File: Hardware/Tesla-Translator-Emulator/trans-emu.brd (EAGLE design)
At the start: 29 x 34 mm, 41 parts, among them IC1 MIC5233-3.3YM5-TR, Q1 PMOSFET, Q2 NMOSFET, U1 STM32F413RGT6, U2 TJA1042HVSON, U3 TJA1042HVSON, U4 TJA1042HVSON, Y1 CRYSTAL-3.2X2.54-PIN

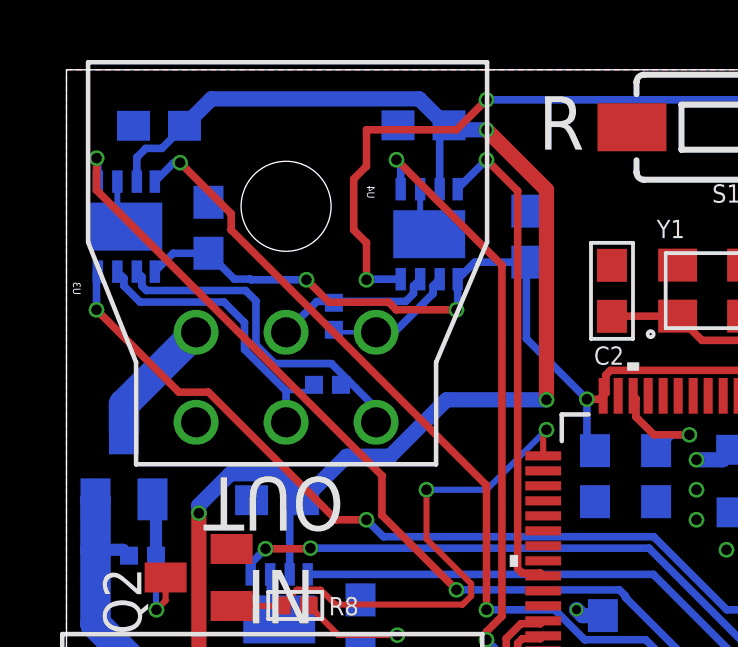
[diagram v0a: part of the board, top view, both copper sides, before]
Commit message: ibooster v2, stm32teensy work
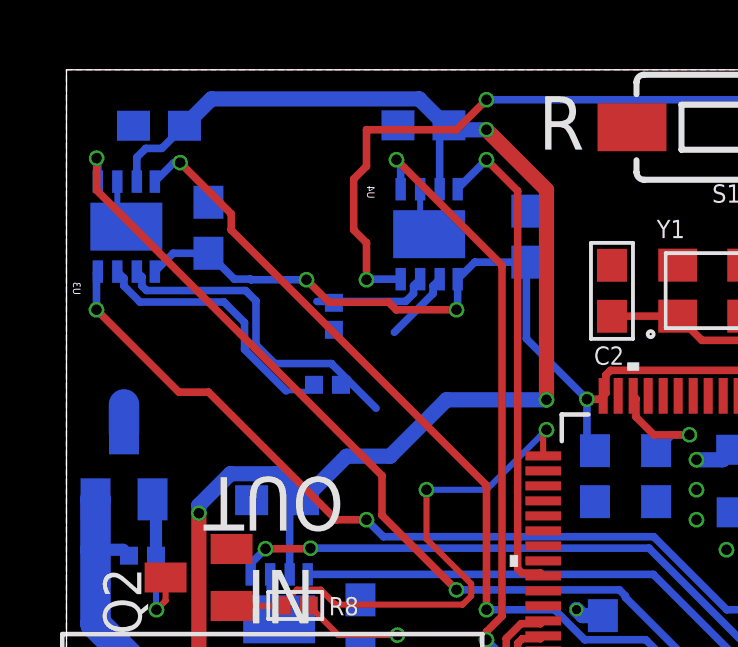
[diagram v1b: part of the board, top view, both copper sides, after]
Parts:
- removed U$2: MICROFIT-6, interceptor:MICROFIT-6
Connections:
- net CAN2_H: no longer U$2.2
- net CAN2_L: no longer U$2.3
- net CAN3_H: no longer U$2.5
- net CAN3_L: no longer U$2.6
- net GND: no longer U$2.1
- net N$15: no longer U$2.4
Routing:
- net N$15: track 4.36 -> 0.97 mm
- net CAN3_L: track 4.44 -> 2.40 mm
- net CAN3_H: track 5.46 -> 3.94 mm
- net CAN2_H: track 10.0 -> 8.97 mm
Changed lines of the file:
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@@
 </element>
 <element name="U$1" library="interceptor" package="MINI50" value="MINI50-4" x="9.86" y="12.19" smashed="yes" rot="R180"/>
-<element name="U$2" library="interceptor" package="MICROFIT-6" value="MICROFIT-6" x="7.32" y="22.25" smashed="yes" rot="R180"/>
 <element name="U1" library="interceptor" package="LQFP64-10X10MM" value="STM32F413RGT6" x="21.64" y="17.38" smashed="yes" rot="R180">
 <attribute name="BUILT_BY" value="EMA_UL_Team" x="-19" y="25" size="1.778" layer="27" rot="R180" display="off"/>
@@
 <contactref element="C14" pad="2"/>
 <contactref element="C12" pad="2"/>
-<contactref element="U$2" pad="1"/>
 <contactref element="IC1" pad="2"/>
 <contactref element="PS1" pad="2"/>
@@
 <wire x1="6.170878125" y1="19.65268125" x2="5.50338125" y2="18.02668125" width="0" layer="19" extent="1-16"/>
 <wire x1="9.86" y1="12.19" x2="11" y2="15" width="0" layer="19" extent="16-16"/>
-<wire x1="4.32" y1="22.25" x2="6.170878125" y2="19.65268125" width="0" layer="19" extent="16-16"/>
 <wire x1="7.278778125" y1="1.89358125" x2="12.39" y2="3.61" width="0" layer="19" extent="16-16"/>
 <wire x1="5.8147" y1="5.02721875" x2="7.278778125" y2="1.89358125" width="0" layer="19" extent="16-16"/>
@@
 <signal name="CAN2_H">
 <contactref element="U3" pad="7"/>
-<contactref element="U$2" pad="2"/>
 <wire x1="1.6952625" y1="27.27271875" x2="1.9162625" y2="27.05171875" width="0.254" layer="16"/>
 <wire x1="1.9162625" y1="27.05171875" x2="1.9162625" y2="26.79250625" width="0.254" layer="16"/>
@@
 <wire x1="5.25018125" y1="26.25851875" x2="5.935" y2="25.5737" width="0.254" layer="16"/>
 <wire x1="5.935" y1="25.5737" x2="5.935" y2="24.67630625" width="0.254" layer="16"/>
-<wire x1="7.32" y1="23.29130625" x2="7.32" y2="22.25" width="0.254" layer="16"/>
 <wire x1="5.935" y1="24.67630625" x2="7.32" y2="23.29130625" width="0.254" layer="16"/>
 <contactref element="R5" pad="1"/>
@@
 <signal name="CAN2_L">
 <contactref element="U3" pad="6"/>
-<contactref element="U$2" pad="3"/>
 <wire x1="2.3452625" y1="27.27271875" x2="2.5162625" y2="27.10171875" width="0.254" layer="16"/>
 <wire x1="2.5162625" y1="27.10171875" x2="2.5162625" y2="26.79250625" width="0.254" layer="16"/>
@@
 <wire x1="6.942225" y1="24.2079" x2="8.829878125" y2="24.2079" width="0.254" layer="16"/>
 <wire x1="6.316" y1="26.2976" x2="6.316" y2="24.834125" width="0.254" layer="16"/>
-<wire x1="10.32" y1="22.25" x2="10.32" y2="22.717778125" width="0.254" layer="16"/>
 <wire x1="10.32" y1="22.717778125" x2="9.364978125" y2="23.6728" width="0.254" layer="16"/>
 <contactref element="R5" pad="2"/>
@@
 <signal name="CAN3_H">
 <contactref element="U4" pad="7"/>
-<contactref element="U$2" pad="5"/>
 <wire x1="11.79" y1="27.02" x2="11.569" y2="26.799" width="0.254" layer="16"/>
 <wire x1="11.569" y1="26.799" x2="11.569" y2="26.5397875" width="0.254" layer="16"/>
 <wire x1="11.569" y1="26.5397875" x2="11.308053125" y2="26.278840625" width="0.254" layer="16"/>
-<wire x1="8.348840625" y1="26.278840625" x2="7.32" y2="25.25" width="0.254" layer="16"/>
 <wire x1="11.308053125" y1="26.278840625" x2="9" y2="26.278840625" width="0.254" layer="16"/>
+<wire x1="9" y1="26.278840625" x2="8.348840625" y2="26.278840625" width="0.254" layer="16"/>
+<wire x1="8.960459375" y1="26.278840625" x2="9" y2="26.278840625" width="0.1524" layer="16"/>
 <contactref element="R6" pad="1"/>
-<wire x1="9" y1="26.278840625" x2="8.348840625" y2="26.278840625" width="0.254" layer="16"/>
-<wire x1="8.9144" y1="26.23278125" x2="8.960459375" y2="26.278840625" width="0.1524" layer="16"/>
-<wire x1="8.960459375" y1="26.278840625" x2="9" y2="26.278840625" width="0.1524" layer="16"/>
+<wire x1="8.9144" y1="26.23278125" x2="8.960459375" y2="26.278840625" width="0" layer="19" extent="16-16"/>
 </signal>
 <signal name="CAN3_L">
 <contactref element="U4" pad="6"/>
-<contactref element="U$2" pad="6"/>
 <wire x1="12.44" y1="27.02" x2="12.219" y2="26.799" width="0.254" layer="16"/>
 <wire x1="12.219" y1="26.799" x2="12.219" y2="26.5397875" width="0.254" layer="16"/>
 <wire x1="12.219" y1="26.5397875" x2="10.9292125" y2="25.25" width="0.254" layer="16"/>
-<wire x1="10.9292125" y1="25.25" x2="10.32" y2="25.25" width="0.254" layer="16"/>
 <contactref element="R6" pad="2"/>
-<wire x1="10.32" y1="25.25" x2="8.99718125" y2="25.25" width="0.1524" layer="16"/>
-<wire x1="8.99718125" y1="25.25" x2="8.9144" y2="25.33278125" width="0.1524" layer="16"/>
+<wire x1="8.9144" y1="25.33278125" x2="10.9292125" y2="25.25" width="0" layer="19" extent="16-16"/>
 </signal>
 <signal name="N$2">
@@
 </signal>
 <signal name="N$15">
-<contactref element="U$2" pad="4"/>
 <contactref element="Q1" pad="3"/>
 <wire x1="1.917440625" y1="21.88231875" x2="1.917440625" y2="22.847440625" width="1.016" layer="16"/>
-<wire x1="1.917440625" y1="22.847440625" x2="4.32" y2="25.25" width="1.016" layer="16"/>
 </signal>
 <signal name="PWRON">

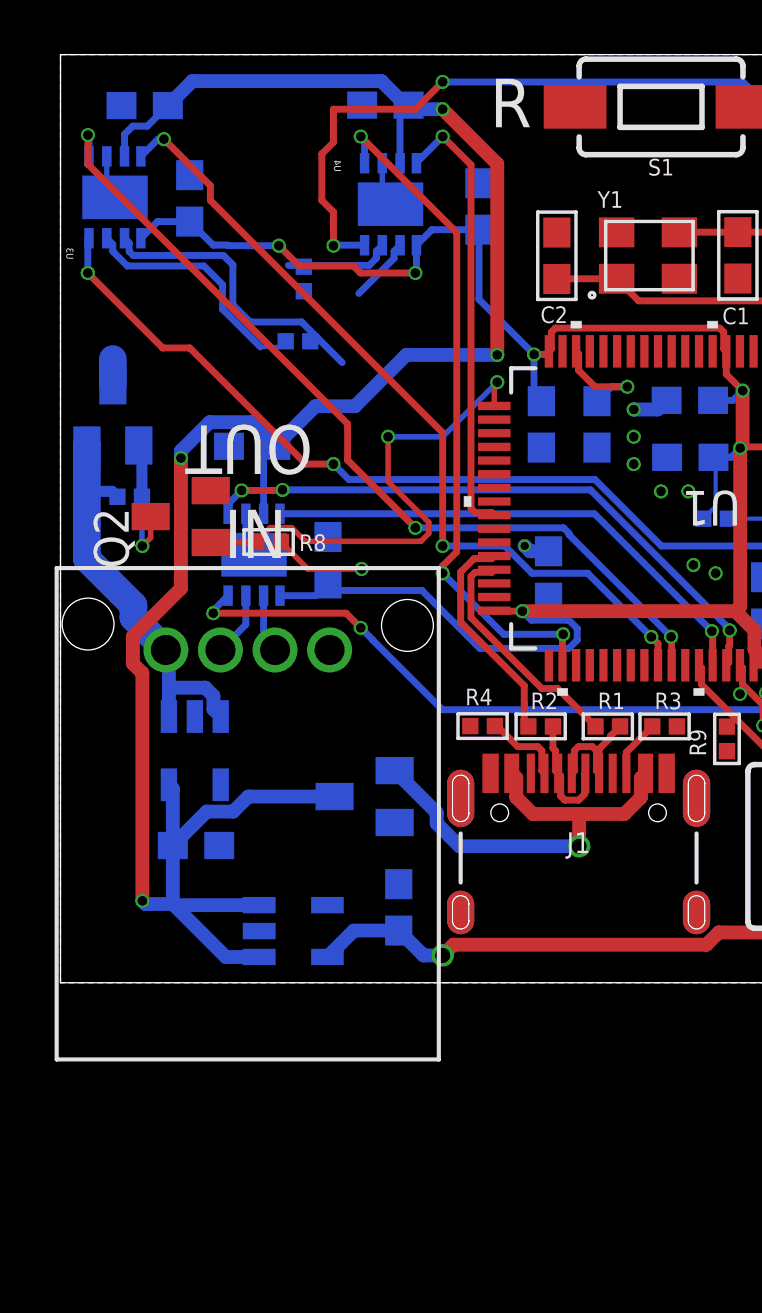
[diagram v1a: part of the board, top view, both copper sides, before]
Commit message: Ibooster board updates
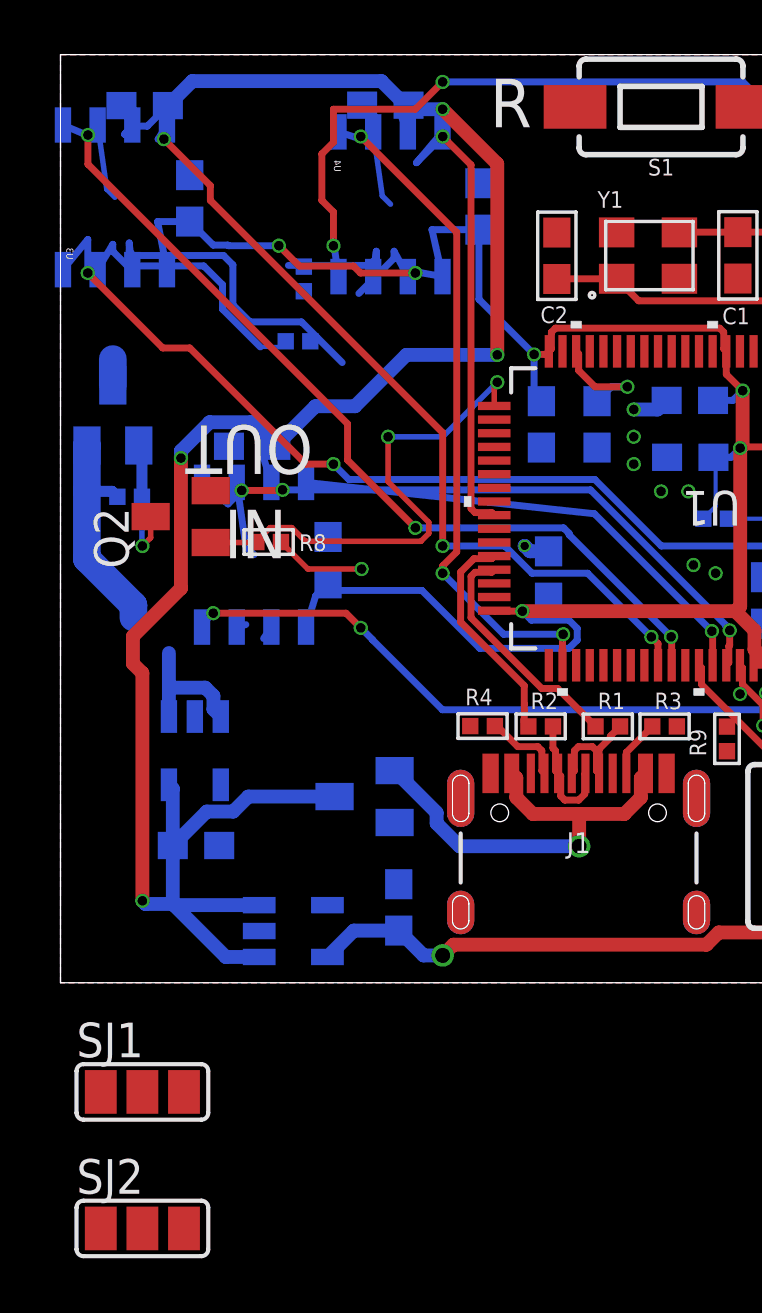
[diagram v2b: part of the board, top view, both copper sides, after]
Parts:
- removed U$1: MINI50-4, interceptor:MINI50
- added SJ1, SJ2: (no value), jumper:SJ_2
- U2, U3, U4: value TJA1042HVSON -> TJA1042; device comma.ai:HVSON8 -> CM,118:NXP_SEMICONDUCTORS_TJA1042T-3-CM_118_0
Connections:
- new net CAN1_H: SJ1.1, U2.7
- new net CAN1_L: SJ2.1, U2.6
- net 12V: no longer U$1.4
- net CAN3_H: now also SJ1.3
- net CAN3_L: now also SJ2.3
- net GND: no longer U$1.1, U2.PAD, U3.PAD, U4.PAD
- net N$12: now also SJ1.2; no longer U$1.3, U2.7
- net N$14: now also SJ2.2; no longer U$1.2, U2.6
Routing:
- net GND: track 13.3 -> 16.8 mm
- net 5V: track 78.9 -> 76.3 mm
- net N$12: track 2.38 -> 0.00 mm
- net N$14: track 2.16 -> 0.00 mm
- net 12V: track 15.0 -> 13.2 mm
- net 3.3V: track 106.6 -> 108.4 mm
- net CAN3_RX: track 16.4 -> 17.8 mm
- net CAN2_EN: track 33.2 -> 34.6 mm
- net CAN1_RX: track 18.9 -> 18.0 mm
- net CAN1_TX: track 22.4 -> 23.3 mm
- net CAN2_H: track 8.97 -> 9.74 mm
- net CAN3_L: track 2.40 -> 3.14 mm
- net CAN2_L: track 11.2 -> 11.9 mm
- net CAN3_H: track 3.94 -> 4.56 mm
- net CAN1_L: track 0.00 -> 0.51 mm

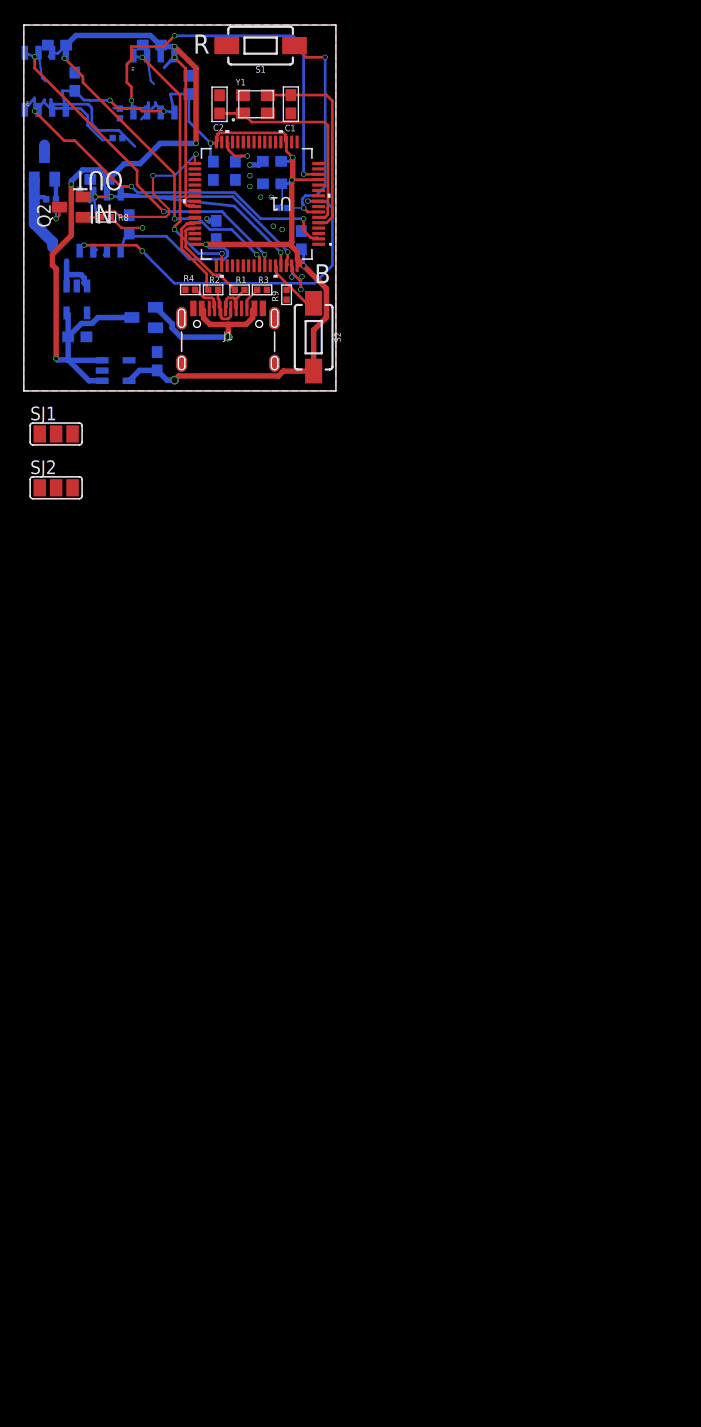
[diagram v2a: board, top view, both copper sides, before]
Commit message: ibooster schematic and water controller
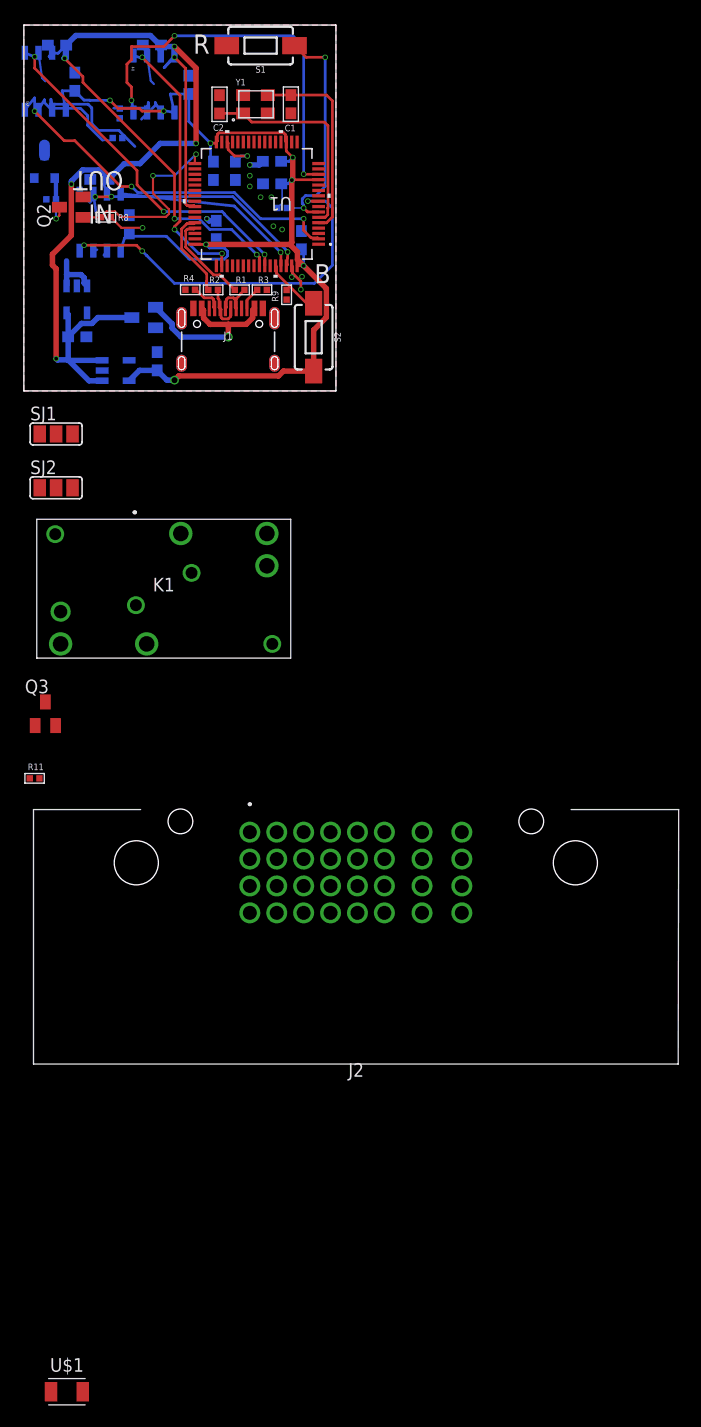
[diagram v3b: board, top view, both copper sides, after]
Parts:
- added J2: 64334-0100, 64334-0100:643340100
- added K1: V23086C2001A403, SamacSys_Parts:V23086C2001A403
- added Q3: NMOSFET, Transistor:SOT23
- added R11: 10k, comma.ai:0402-R
- added U$1: FUSE_CHIP-1206(3216-METRIC), Circuit-Protection:FUSC3215X82N
- Q1: value PMOSFET -> 4.3A/20V/54mΩ; device Transistor:SOT23 -> SparkFun-DiscreteSemi:SOT23-3
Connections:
- removed net N$15: Q1.3
- new net BLIGHT: Q3.1, R11.2, U1.34
- new net COM1: J2.A2, K1.14
- new net COM2: J2.B2, K1.24
- new net IBSTIN: J2.H1, Q1.2, R7.2
- new net IBSTOUT: Q1.3, U$1.2
- new net N$17: K1.11, K1.21, Q3.3
- new net N$18: J2.G1, U$1.1
- new net NC1: J2.A1, K1.13
- new net NC2: J2.B1, K1.23
- new net NO1: J2.A3, K1.15
- new net NO2: J2.B3, K1.25
- net 12V: now also J2.C1, K1.12, K1.22; no longer Q1.2, R7.2
- net CAN1_H: now also J2.C2
- net CAN1_L: now also J2.C3
- net CAN2_H: now also J2.E2
- net CAN2_L: now also J2.E1
- net GND: now also J2.C4, J2.G2, J2.H2, Q3.2, R11.1
- net N$12: now also J2.F2
- net N$14: now also J2.F1
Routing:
- net 12V: track 13.2 -> 4.95 mm
- net N$15: track 0.97 -> 0.00 mm
- net IBSTOUT: track 0.00 -> 0.97 mm
